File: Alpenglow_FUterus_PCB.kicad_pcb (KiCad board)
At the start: 2 copper layers, 76.2 x 76.2 mm, 14 parts

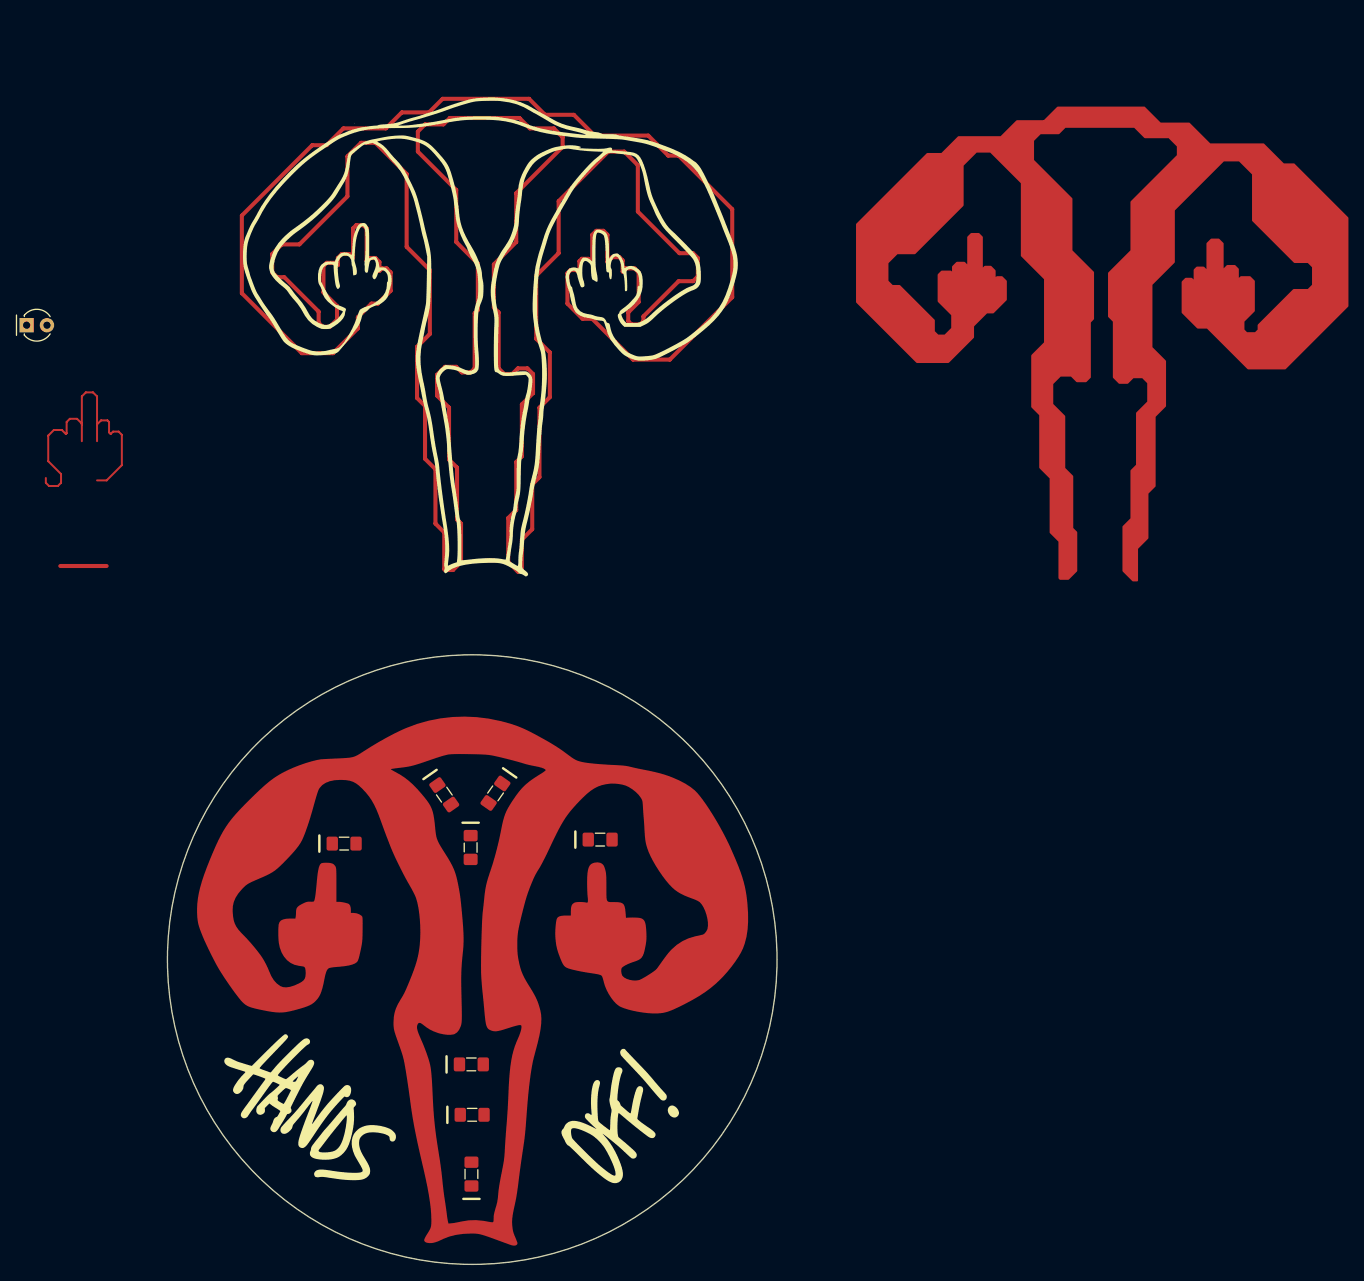
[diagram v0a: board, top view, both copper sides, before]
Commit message: Added easyeda library and LED side mount pattern, updated PCB, aligned uterus copper & mask
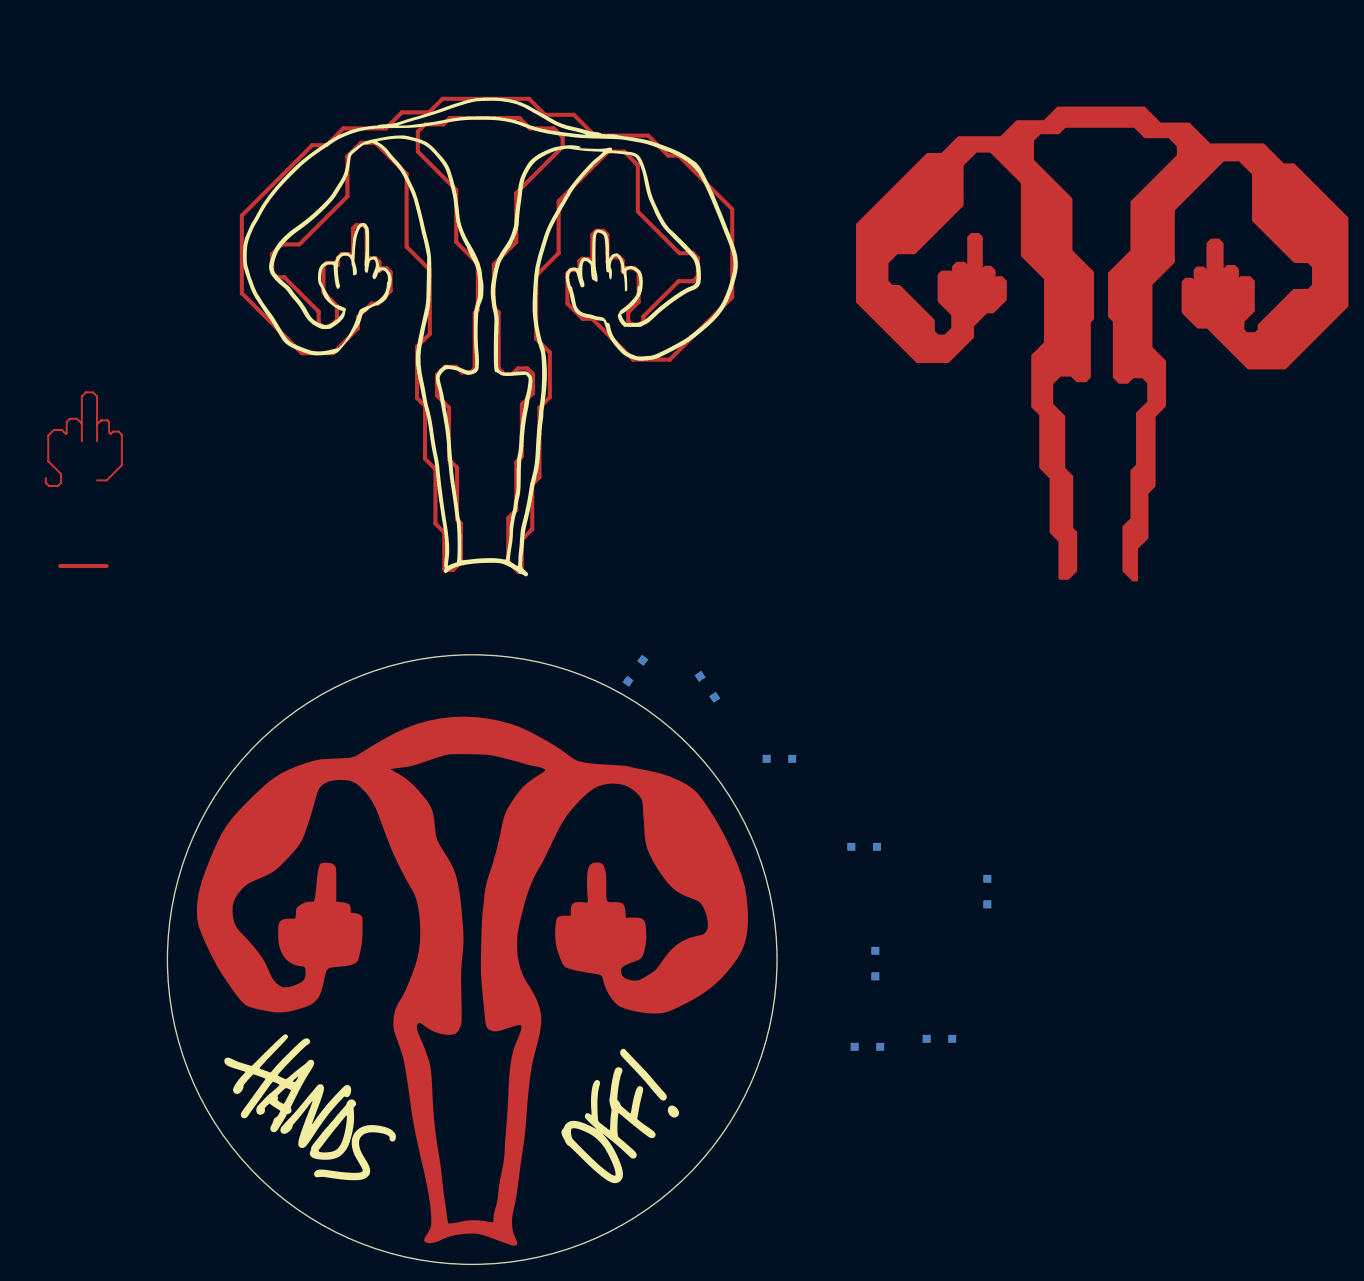
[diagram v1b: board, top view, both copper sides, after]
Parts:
- removed the D1 at (97.9, 84.8)
- D1, D2, D3, D4, D5, D6, D7, D8: footprint Alpenglow:LED_1206+ -> easyeda2kicad:LED-SMD_L3.8-W1.0-R-RD_RED; moved to B.Cu
- G***: value LOGO -> UterusSoldermask
- G***: value LOGO -> Uterus Copper
- moved D4 73.5 mm to (218.0, 155.6)
- moved D6 65.0 mm to (202.6, 150.0), turned to 180 degrees
- moved D1 59.2 mm to (212.0, 174.0), turned to 180 degrees
- moved D8 52.6 mm to (204.0, 164.6)
- moved D3 49.6 mm to (203.0, 175.0), turned to 180 degrees
- moved D7 29.7 mm to (183.0, 130.0), turned to -55 degrees
- moved D2 28.5 mm to (174.0, 128.0), turned to -125 degrees
- moved D5 24.6 mm to (192.0, 139.0), turned to 180 degrees
- moved G*** 0.10 mm to (153.1, 163.8)

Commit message: deleted old alternate graphics
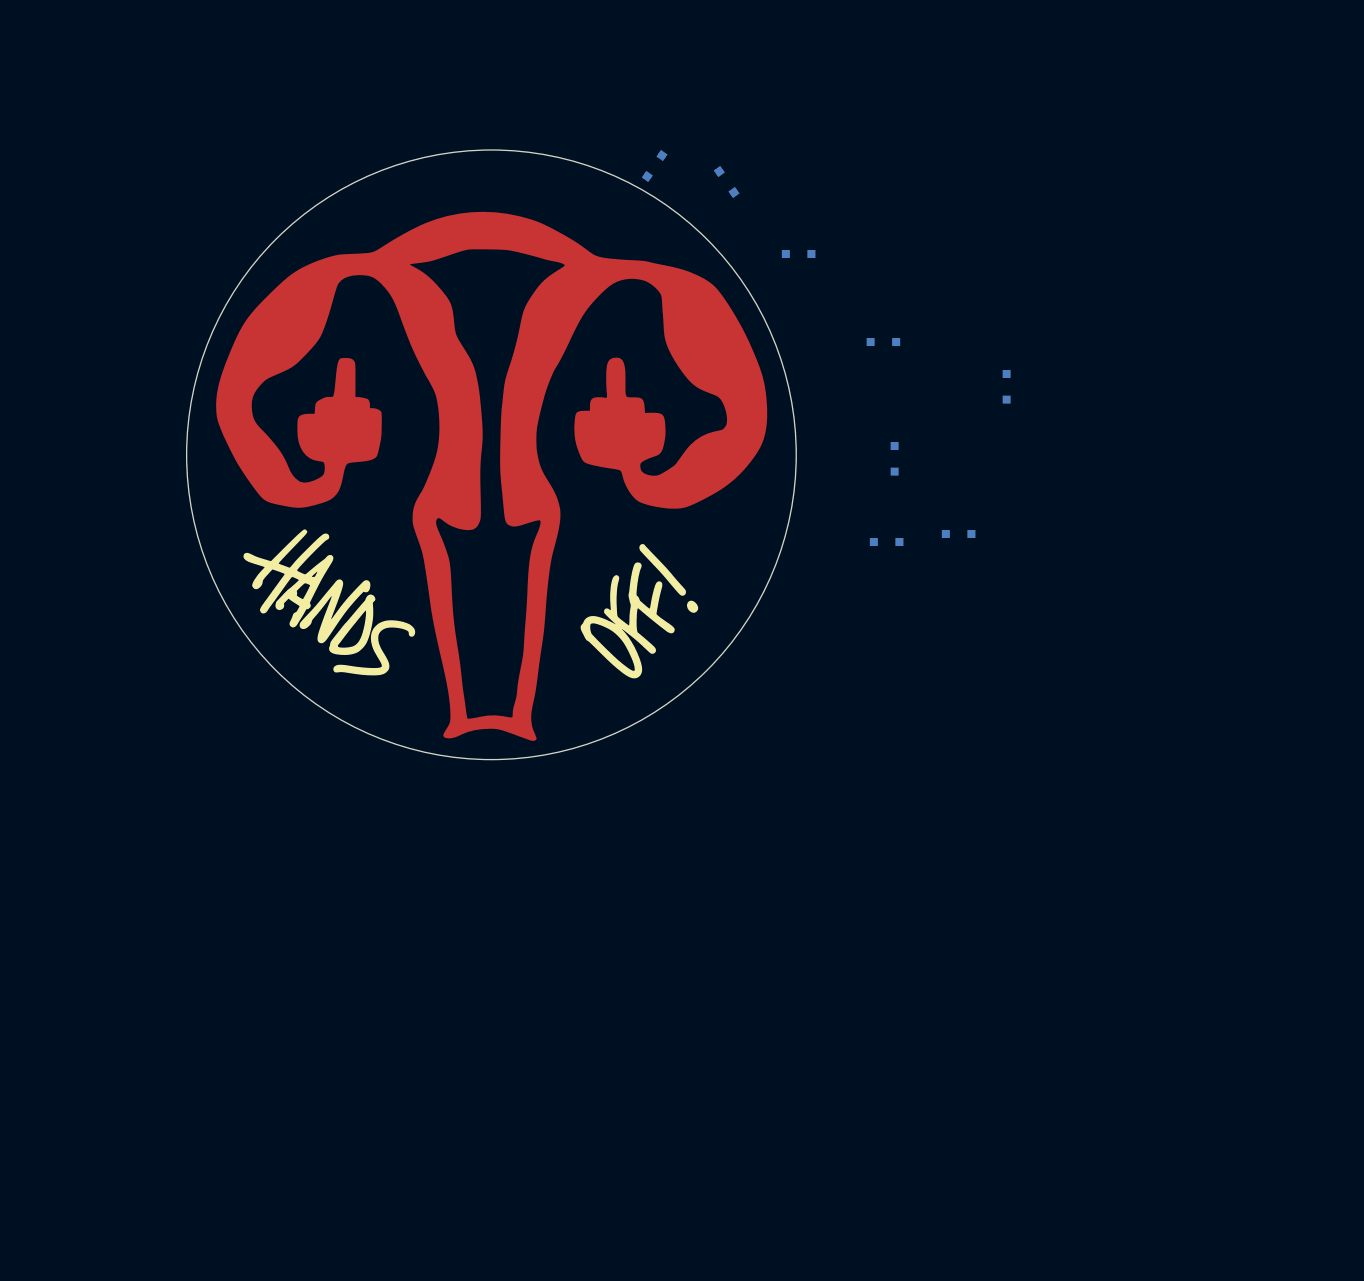
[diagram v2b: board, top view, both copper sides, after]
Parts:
- removed the G*** at (155.9, 86.2)
- moved D1 63.1 mm to (214.4, 110.9)
- moved D2 63.1 mm to (176.4, 64.9)
- moved D3 63.1 mm to (205.4, 111.9)
- moved D4 63.1 mm to (220.4, 92.5)
- moved D5 63.1 mm to (194.4, 75.9)
- moved D6 63.1 mm to (205.0, 86.9)
- moved D7 63.1 mm to (185.4, 66.9)
- moved D8 63.1 mm to (206.4, 101.5)
- moved G*** 63.1 mm to (135.9, 120.1)
- moved G*** 63.1 mm to (155.5, 100.7) (x2)
- moved G*** 63.1 mm to (173.6, 120.5)
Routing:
- net (no net): track 586.3 -> 0.00 mm

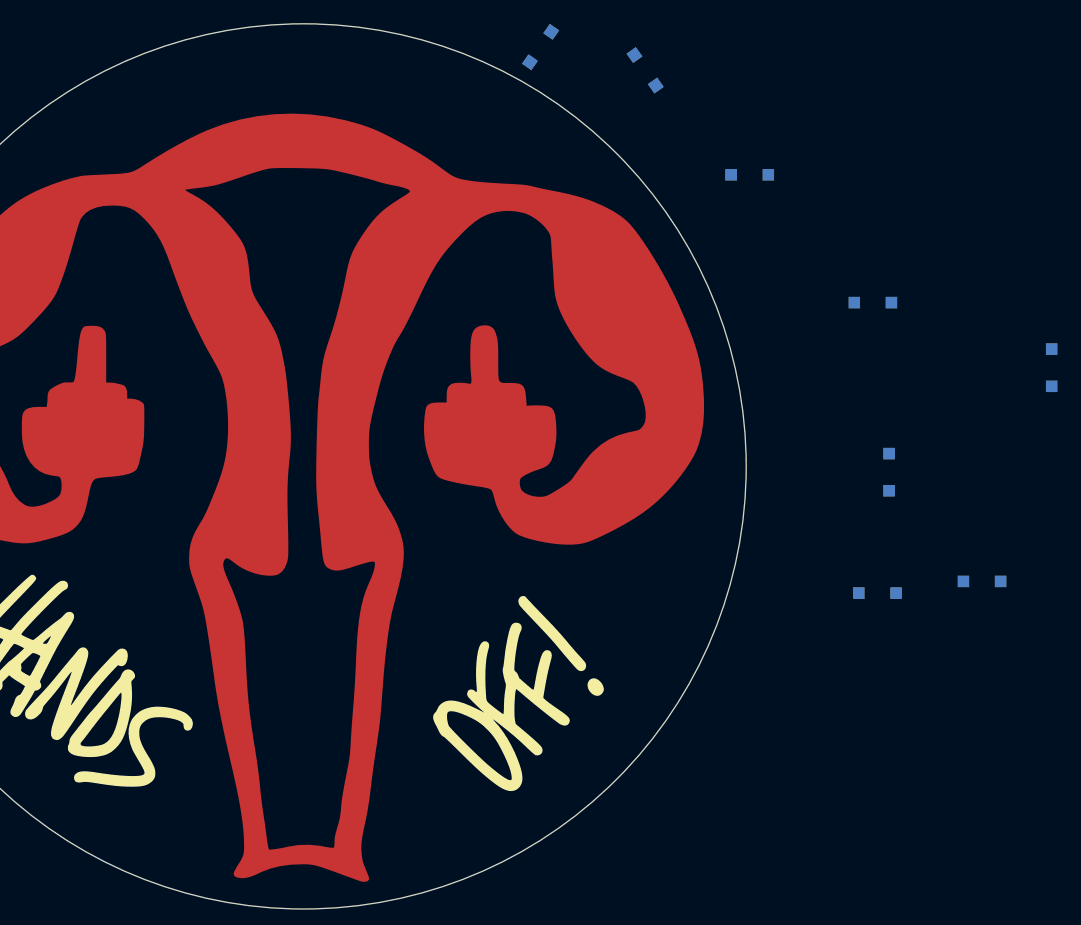
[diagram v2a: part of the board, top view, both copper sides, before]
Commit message: still a WIP, working on main component placement, considering processor vs self-blinking LEDs
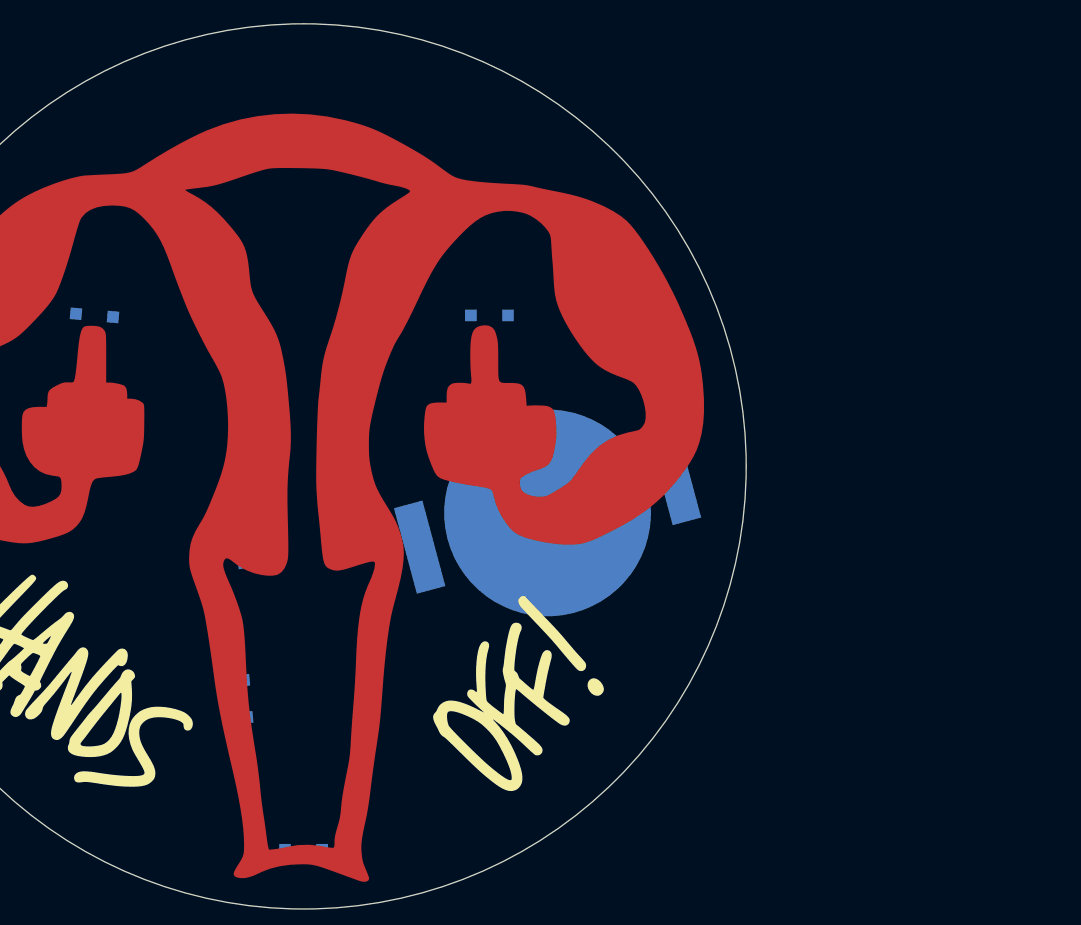
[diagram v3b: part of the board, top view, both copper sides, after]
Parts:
- added BT1: Battery_Cell, Alpenglow:BatteryHolder_CR2032_SMT, B.Cu at (177.0, 105.0)
- added D10: LED, easyeda2kicad:LED-SMD_L3.8-W1.0-R-RD_RED, B.Cu at (151.0, 86.0)
- added D11: LED, easyeda2kicad:LED-SMD_L3.8-W1.0-R-RD_RED, B.Cu at (138.0, 88.0)
- added D12: LED, easyeda2kicad:LED-SMD_L3.8-W1.0-R-RD_RED, B.Cu at (172.0, 88.0)
- added D9: LED, easyeda2kicad:LED-SMD_L3.8-W1.0-R-RD_RED, B.Cu at (152.4, 109.0)
- moved D1 73.5 mm to (150.0, 75.5), turned to 20 degrees
- moved D7 73.3 mm to (156.0, 134.0), turned to 180 degrees
- moved D4 62.6 mm to (158.0, 97.0), turned to -90 degrees
- moved D8 58.7 mm to (151.0, 121.0), turned to 95 degrees
- moved D6 55.7 mm to (161.0, 121.0), turned to -95 degrees
- moved D3 51.9 mm to (161.0, 85.0), turned to -105 degrees
- moved D5 47.1 mm to (160.0, 108.0), turned to -10 degrees
- moved D2 19.3 mm to (160.0, 75.0), turned to -15 degrees

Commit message: picked it back up and started changes for through-hole kit
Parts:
- removed D10, D11, D12, D4, D5, D6, D7, D8, D9: LED, easyeda2kicad:LED-SMD_L3.8-W1.0-R-RD_RED
- removed the G*** at (155.5, 100.7)
- added REF**: LED_D3.0mm_Horizontal_O3.81mm_Z2.0mm, LED_THT:LED_D3.0mm_Horizontal_O3.81mm_Z2.0mm, F.Cu at (168.5, 49.1)
- added SW1: SW_SLIDE, Alpenglow:SW_SPDT_SLIDE_THRU_RTA, F.Cu at (108.7, 118.2)
- D1, D2, D3: value LED -> RED; footprint easyeda2kicad:LED-SMD_L3.8-W1.0-R-RD_RED -> LED_THT:LED_D5.0mm_Horizontal_O3.81mm_Z3.0mm
- moved D1 40.9 mm to (141.5, 115.5), turned to 10 degrees
- moved D3 30.7 mm to (166.0, 115.2), turned to -10 degrees
- moved BT1 18.3 mm to (173.8, 123.0), turned to 45 degrees
- moved D2 10.2 mm to (156.8, 65.3), turned to 180 degrees
- moved G*** 0.70 mm to (155.5, 100.0)
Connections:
- BT1 pad 1: unconnected-(BT1-+-Pad1) -> /BATT+
- BT1 pad 2: unconnected-(BT1---Pad2) -> GND
- D1 pad 1: unconnected-(D1-K-Pad1) -> GND
- D1 pad 2: unconnected-(D1-A-Pad2) -> /LED+
- D2 pad 1: unconnected-(D2-K-Pad1) -> GND
- D2 pad 2: unconnected-(D2-A-Pad2) -> /LED+
- D3 pad 1: unconnected-(D3-K-Pad1) -> GND
- D3 pad 2: unconnected-(D3-A-Pad2) -> /LED+

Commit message: artwork progress, still needs cleanup
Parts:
- removed the G*** at (135.9, 120.1)
- removed the G*** at (173.6, 120.5)
- removed the REF** at (168.5, 49.1)
- added ?: , clipboard:012cae34-f1dd-4b8d-b211-b91f0b5daded, F.Cu at (178.4, 30.8)
- added ?: , clipboard:e98188f8-7f42-447a-8872-9487c3771e00, F.Cu at (167.0, 107.4)
- added ?: , clipboard:26569cd0-89ac-46e3-aafd-ce9c73fc9669, F.Cu at (207.0, 111.7)
- added ?: , clipboard:8a7704ae-2f3d-4998-8880-3184b098a79f, F.Cu at (205.2, 99.2)
- added ?: , clipboard:1713b159-2950-4087-b007-d83dcec81724, F.Cu at (199.3, 76.9)
- added ?: , clipboard:bf1500f7-63e0-4397-bbdb-e8a181ed9b95, F.Cu at (142.4, 130.2)
- added ?: , clipboard:6fd78f95-30c4-45d5-b97f-0a242345d2c7, F.Cu at (182.8, 122.0)
- added ?: , clipboard:24eddce0-fbb7-42ce-b102-221b78fe7c8a, F.Cu at (242.0, 85.2)
- added R1: RES, Resistor_THT:R_Axial_DIN0207_L6.3mm_D2.5mm_P10.16mm_Horizontal, B.Cu at (145.0, 123.0)
- added REF**: MountingHole_2.5mm, Alpenglow:MountingHole_3.1mm, F.Cu at (155.0, 66.0)
- BT1: value Battery_Cell -> CR2032; footprint Alpenglow:BatteryHolder_CR2032_SMT -> Alpenglow:CR2032_Holder_Clip_Through_Hole-BS-03-A1AJ001
- SW1: moved to B.Cu
- moved D2 68.8 mm to (154.7, 134.2), turned to 0 degrees
- moved D3 48.5 mm to (165.7, 66.7), turned to -155 degrees
- moved D1 47.9 mm to (146.6, 67.8), turned to 155 degrees
- moved SW1 26.2 mm to (133.0, 128.0), turned to 135 degrees
- moved BT1 4.19 mm to (175.0, 119.0), turned to -125 degrees
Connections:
- SW1 pad 3: /LED+ -> Net-(R1-Pad1)
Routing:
- net GND: vias 0 -> 1
- net /LED+: vias 0 -> 1
